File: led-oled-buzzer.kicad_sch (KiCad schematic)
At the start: 17 parts, among them J6 A1250WV-S-4P, Q4 BC847

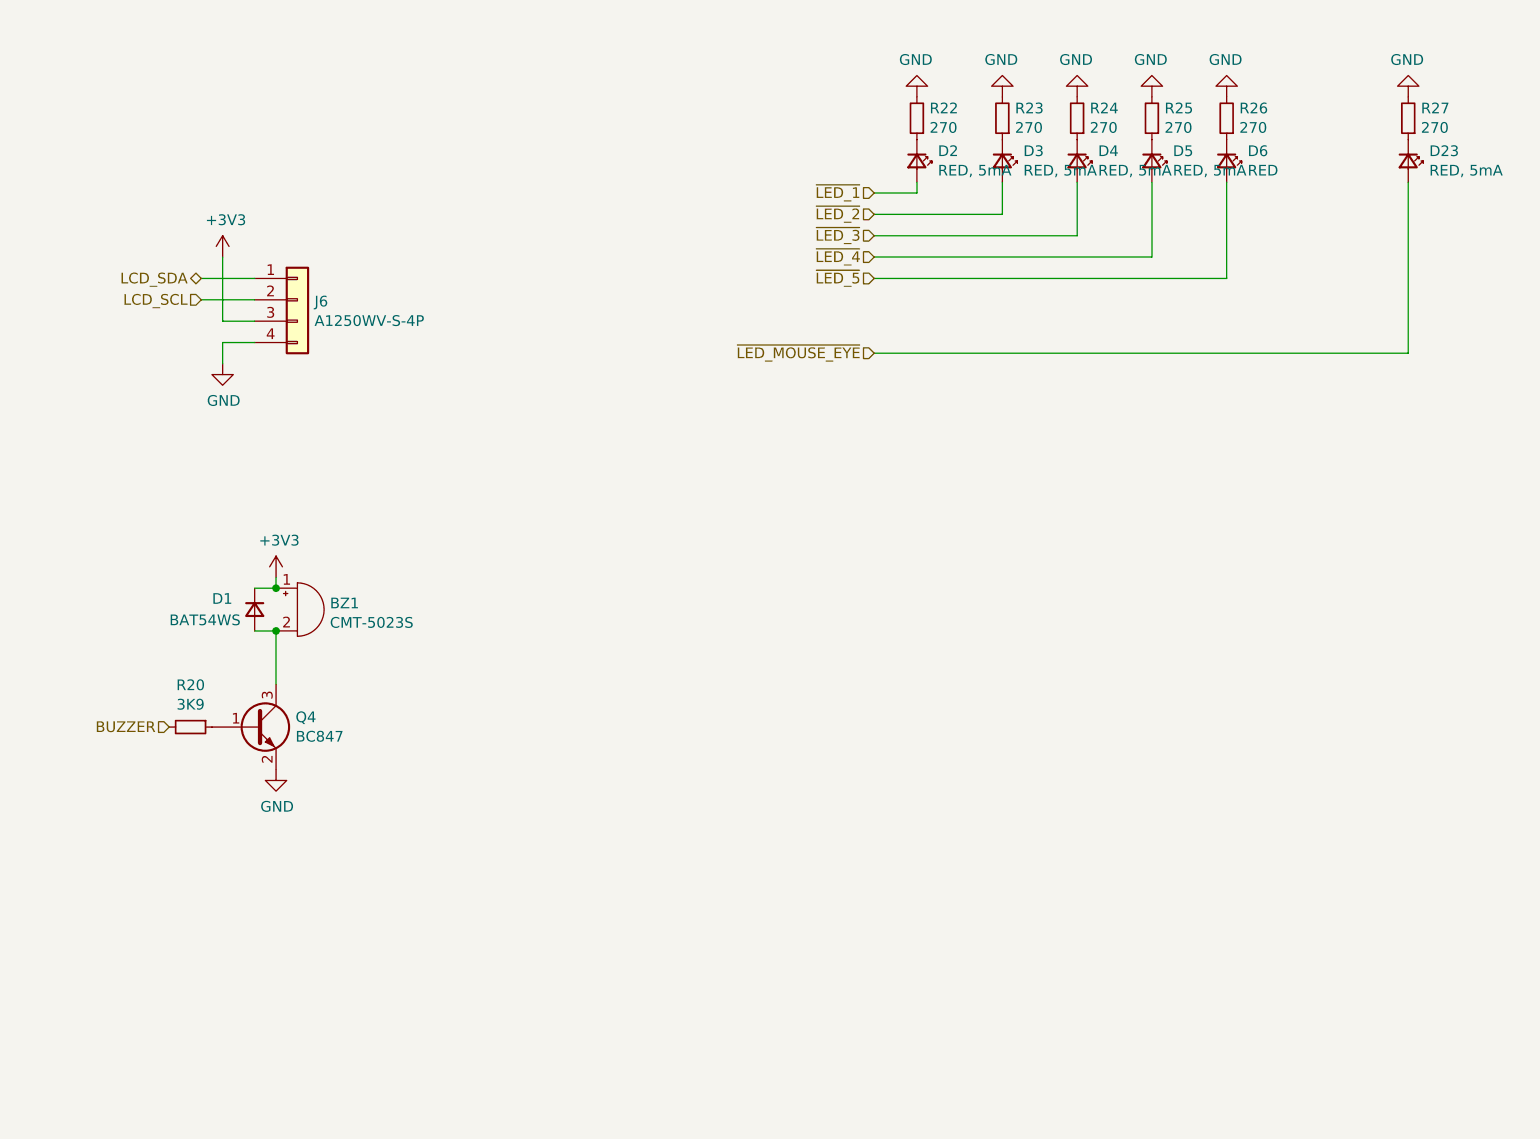
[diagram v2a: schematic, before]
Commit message: Cleanup led-oled schematic
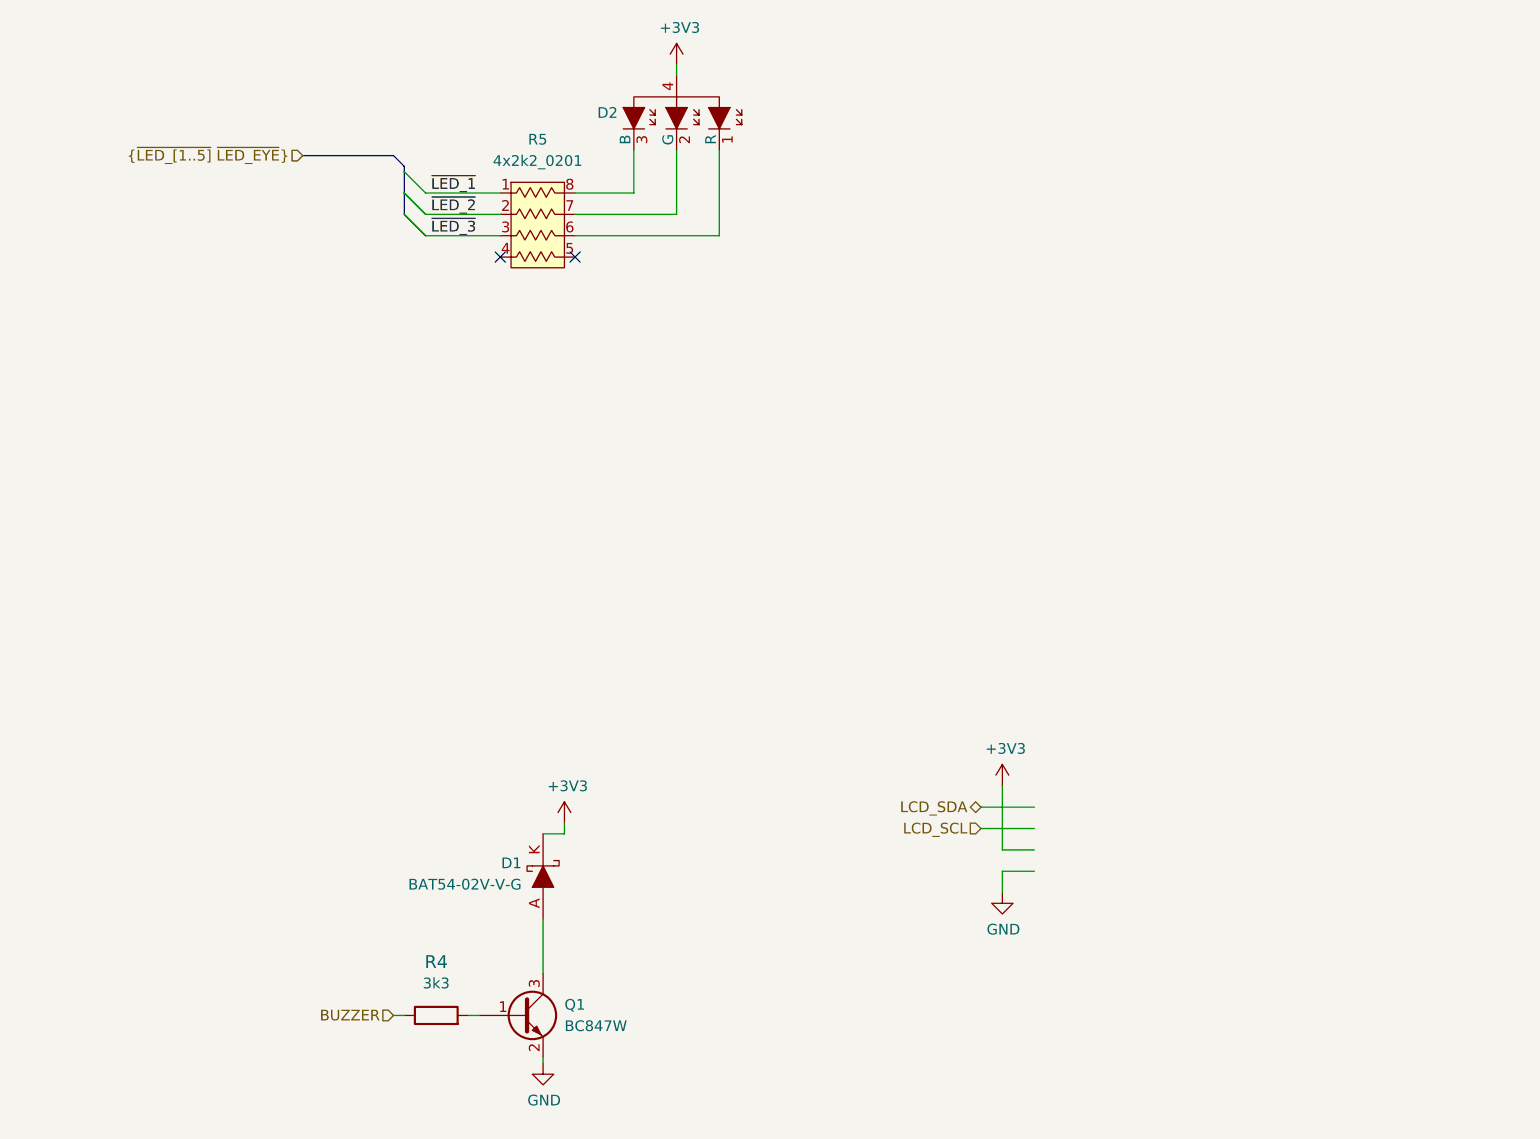
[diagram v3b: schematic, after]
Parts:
- removed BZ1: CMT-5023S, CMT-5023S-SMT-TR:CMT5023SSMTTR, symbol Device:Buzzer
- removed D1: BAT54WS, Diode_SMD:D_SOD-323, symbol Device:D_Small
- removed D2, D23, D3, D4, D5: RED, 5mA, LED_SMD:LED_0402_1005Metric, symbol Device:LED_Small
- removed D6: RED, LED_SMD:LED_0402_1005Metric, symbol Device:LED_Small
- removed J6: A1250WV-S-4P, connector_brd2brd:01x04_1.0x0.5mm_SMD, symbol Connector_Generic:Conn_01x04
- removed Q4: BC847, Package_TO_SOT_SMD:SOT-23, symbol Transistor_BJT:BC847
- removed R20: 3K9, Resistor_SMD:R_0402_1005Metric, symbol Device:R_Small
- removed R22, R23, R24, R25, R26, R27: 270, Resistor_SMD:R_0402_1005Metric, symbol Device:R_Small
- added D1: BAT54-02V-V-G, antmicro-footprints:SOD-523, symbol antmicroDiodesRectifiersSingle:BAT54-02V-V-G
- added D2: LTST-C19HE1WT, antmicro-footprints:LED_Dual0603, symbol antmicroLEDIndicationDiscrete:LTST-C19HE1WT
- added Q1: BC847W, antmicro-footprints:SOT-323, symbol antmicroTransistorsBipolarSingle:BC847W
- added R4: R_3k3_0402, antmicro-footprints:0402-res, symbol antmicroResistors0402:R_3k3_0402
- added R5: 4x2k2_0201_array, antmicro-footprints:EXB18V, symbol antmicroResistorNetworksArrays:4x2k2_0201_array
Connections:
- net +3V3: now also D1.K, D2.4
- net BUZZER: now also R4.1
- net GND: now also Q1.2 (E)
- net ~{LED_1}: now also R5.1
- net ~{LED_2}: now also R5.2
- net ~{LED_3}: now also R5.3
- new net: Q1.1 (B), R4.2
- new net: D1.A, Q1.3 (C)
- new net: D2.1 (R), R5.6
- new net: D2.2 (G), R5.7
- new net: D2.3 (B), R5.8
- no-connect marks 0 -> 2

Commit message: Add buzzer, change diode to 1N4xxx
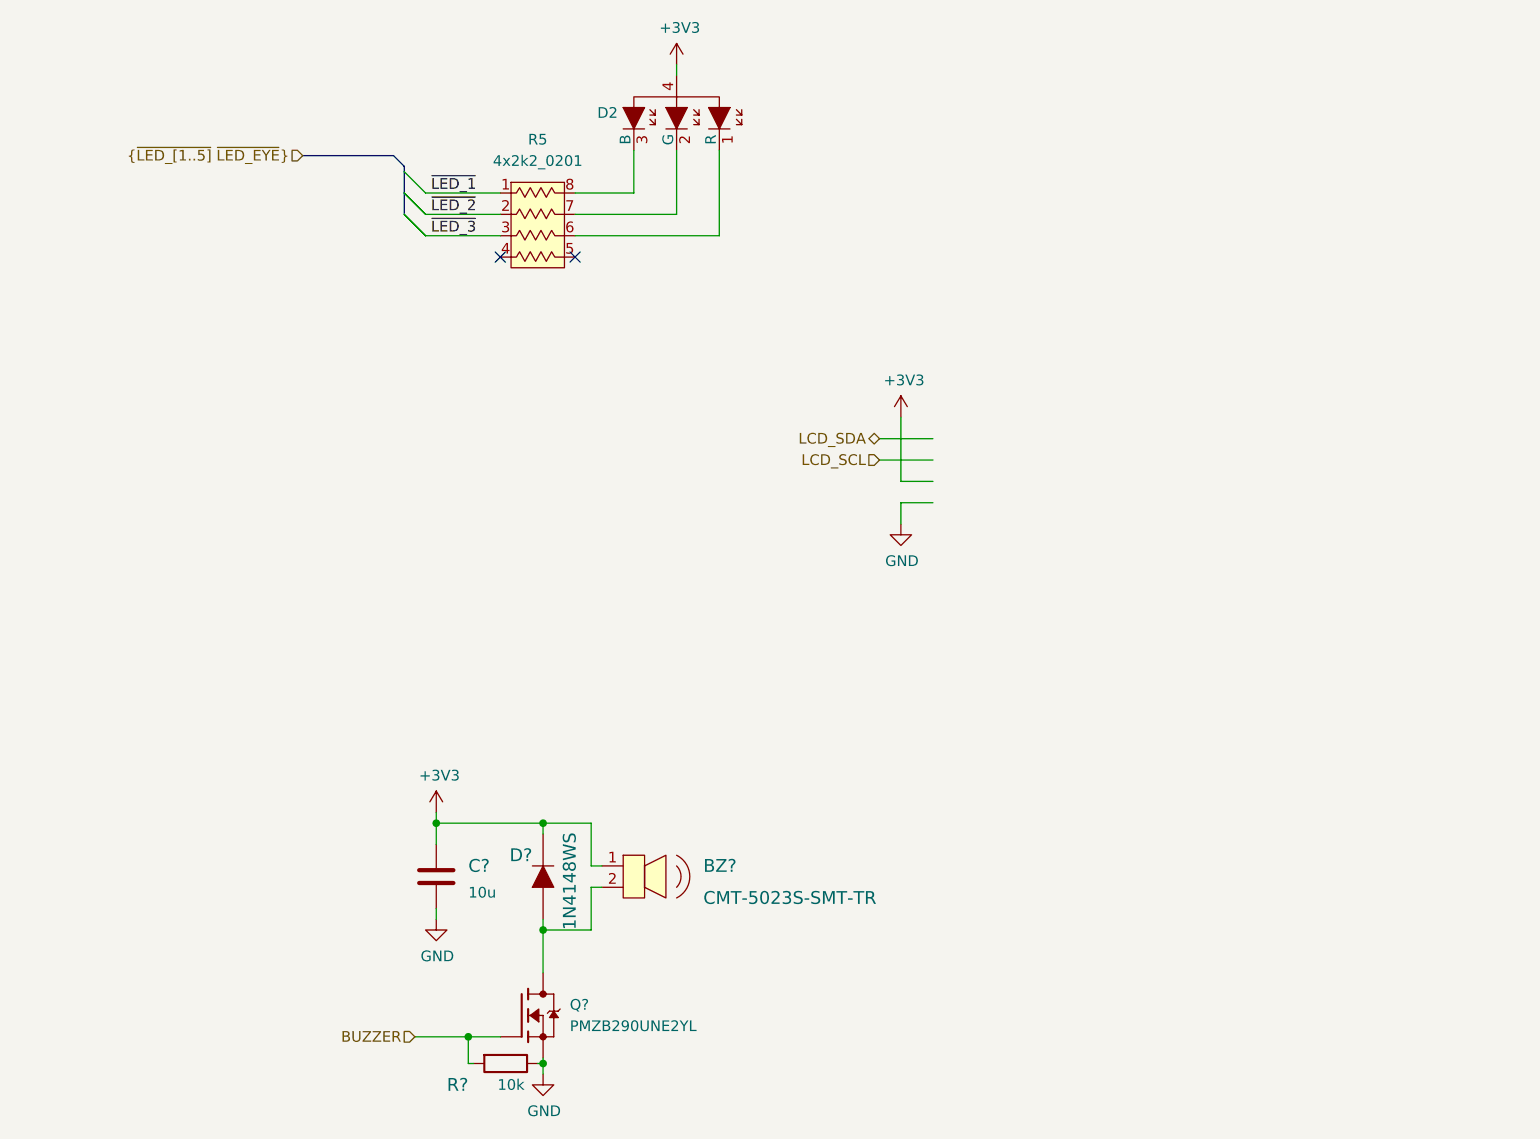
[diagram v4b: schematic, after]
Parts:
- removed D1: BAT54-02V-V-G, antmicro-footprints:SOD-523, symbol antmicroDiodesRectifiersSingle:BAT54-02V-V-G
- removed Q1: BC847W, antmicro-footprints:SOT-323, symbol antmicroTransistorsBipolarSingle:BC847W
- removed R4: R_3k3_0402, antmicro-footprints:0402-res, symbol antmicroResistors0402:R_3k3_0402
- added BZ?: CMT-5023S-SMT-TR, antmicro-footprints:CMT5023SSMTTR, symbol antmicroAlarmsBuzzersandSirens:CMT-5023S-SMT-TR
- added C?: C_10u_0402, antmicro-footprints:0402-cap, symbol antmicroCapacitors0402:C_10u_0402
- added D?: 1N4148WS, antmicro-footprints:SOD-323F, symbol antmicroDiodesRectifiersSingle:1N4148WS
- added Q?: PMZB290UNE2YL, antmicro-footprints:SOT-883, symbol antmicroTransistorsFETsMOSFETsSingle:PMZB290UNE2YL
- added R?: R_10k_0402, antmicro-footprints:0402-res, symbol antmicroResistors0402:R_10k_0402
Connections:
- net +3V3: now also BZ?.1, C?.1, D?.K
- net BUZZER: now also Q?.1 (G), R?.2
- net GND: now also C?.2, Q?.2 (S), R?.1
- new net: BZ?.2, D?.A, Q?.3 (D)

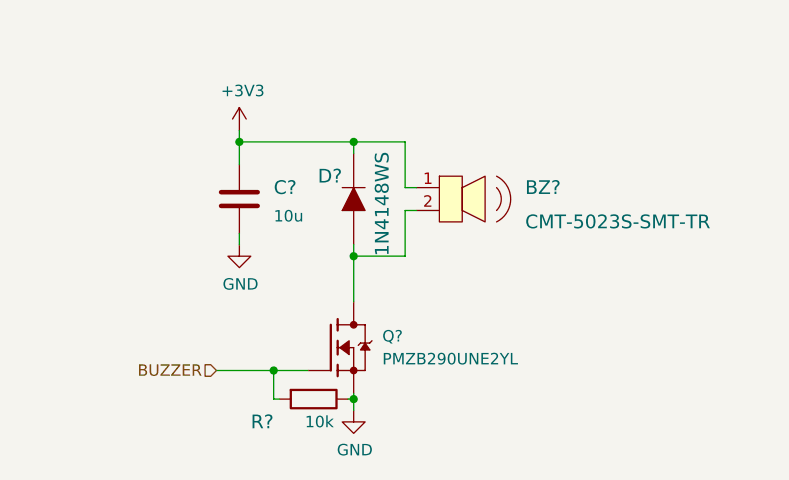
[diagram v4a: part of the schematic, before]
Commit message: Update encoder board pads on PCB
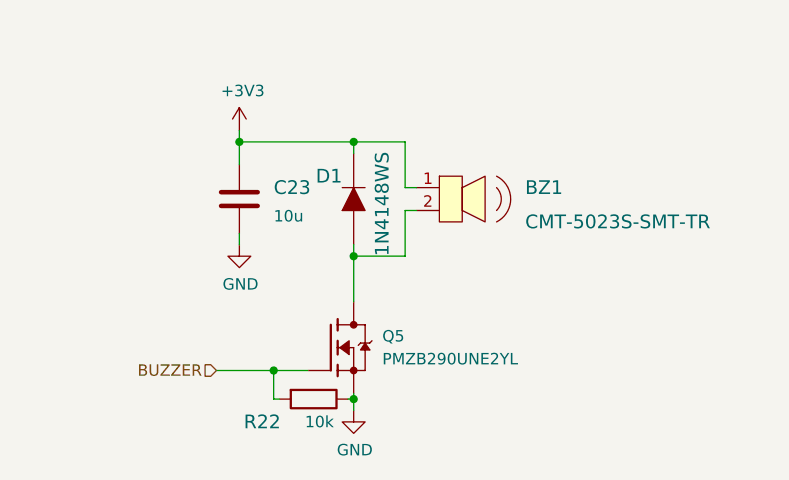
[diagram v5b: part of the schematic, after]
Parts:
- gave numbers to parts that had none: 5
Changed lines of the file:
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@@
   (symbol (lib_id "antmicroTransistorsFETsMOSFETsSingle:PMZB290UNE2YL") (at 120.65 144.78 0) (unit 1)
     (in_bom yes) (on_board yes) (fields_autoplaced)
-    (property "Reference" "Q?" (id 0) (at 126.365 143.5099 0)
+    (property "Reference" "Q5" (id 0) (at 126.365 143.5099 0)
       (effects (font (size 1.27 1.27)) (justify left))
     )
@@
   (symbol (lib_id "antmicroResistors0402:R_10k_0402") (at 118.745 150.495 180) (unit 1)
     (in_bom yes) (on_board yes)
-    (property "Reference" "R?" (id 0) (at 113.03 153.035 0)
+    (property "Reference" "R22" (id 0) (at 113.03 153.035 0)
       (effects (font (size 1.524 1.524)))
     )
@@
   (symbol (lib_id "power:GND") (at 110.49 133.35 0) (unit 1)
     (in_bom yes) (on_board yes)
-    (property "Reference" "#PWR?" (id 0) (at 110.49 139.7 0)
+    (property "Reference" "#PWR0150" (id 0) (at 110.49 139.7 0)
       (effects (font (size 1.27 1.27)) hide)
     )
@@
   (symbol (lib_id "antmicroCapacitors0402:C_10u_0402") (at 110.49 128.27 0) (unit 1)
     (in_bom yes) (on_board yes) (fields_autoplaced)
-    (property "Reference" "C?" (id 0) (at 114.3 127 0)
+    (property "Reference" "C23" (id 0) (at 114.3 127 0)
       (effects (font (size 1.524 1.524)) (justify left))
     )
@@
   (symbol (lib_id "antmicroAlarmsBuzzersandSirens:CMT-5023S-SMT-TR") (at 132.715 129.54 0) (unit 1)
     (in_bom yes) (on_board yes) (fields_autoplaced)
-    (property "Reference" "BZ?" (id 0) (at 142.24 127 0)
+    (property "Reference" "BZ1" (id 0) (at 142.24 127 0)
       (effects (font (size 1.524 1.524)) (justify left))
     )
@@
   (symbol (lib_id "antmicroDiodesRectifiersSingle:1N4148WS") (at 123.19 128.27 90) (unit 1)
     (in_bom yes) (on_board yes)
-    (property "Reference" "D?" (id 0) (at 121.92 125.73 90)
+    (property "Reference" "D1" (id 0) (at 121.92 125.73 90)
       (effects (font (size 1.524 1.524)) (justify left))
     )

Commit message: Loclib, cleanup
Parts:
- BZ1: footprint antmicro-footprints:CMT5023SSMTTR -> synermycha-electronics-footprints:CMT5023SSMTTR; symbol antmicroAlarmsBuzzersandSirens:CMT-5023S-SMT-TR -> synermycha-electronics:CMT-5023S-SMT-TR
- C23: footprint antmicro-footprints:0402-cap -> synermycha-electronics-footprints:0402-cap; symbol antmicroCapacitors0402:C_10u_0402 -> synermycha-electronics:C_10u_0402
- D1: footprint antmicro-footprints:SOD-323F -> synermycha-electronics-footprints:SOD-323F; symbol antmicroDiodesRectifiersSingle:1N4148WS -> synermycha-electronics:1N4148WS
- D2: footprint antmicro-footprints:LED_Dual0603 -> synermycha-electronics-footprints:LED_Dual0603; symbol antmicroLEDIndicationDiscrete:LTST-C19HE1WT -> synermycha-electronics:LTST-C19HE1WT
- Q5: footprint antmicro-footprints:SOT-883 -> synermycha-electronics-footprints:SOT-883; symbol antmicroTransistorsFETsMOSFETsSingle:PMZB290UNE2YL -> synermycha-electronics:PMZB290UNE2YL
- R22: footprint antmicro-footprints:0402-res -> synermycha-electronics-footprints:0402-res; symbol antmicroResistors0402:R_10k_0402 -> synermycha-electronics:R_10k_0402
- R5: footprint antmicro-footprints:EXB18V -> synermycha-electronics-footprints:EXB18V; symbol antmicroResistorNetworksArrays:4x2k2_0201_array -> synermycha-electronics:4x2k2_0201_array
